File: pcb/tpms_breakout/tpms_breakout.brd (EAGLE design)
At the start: 50.8 x 61 mm, 21 parts, among them P1 53398-0410, P2 53398-0410, P3 53398-0410, P4 53398-0410, P5 53398-0410, P6 53398-0410, P7 53398-0410, P8 53398-0410, P9 53398-0610

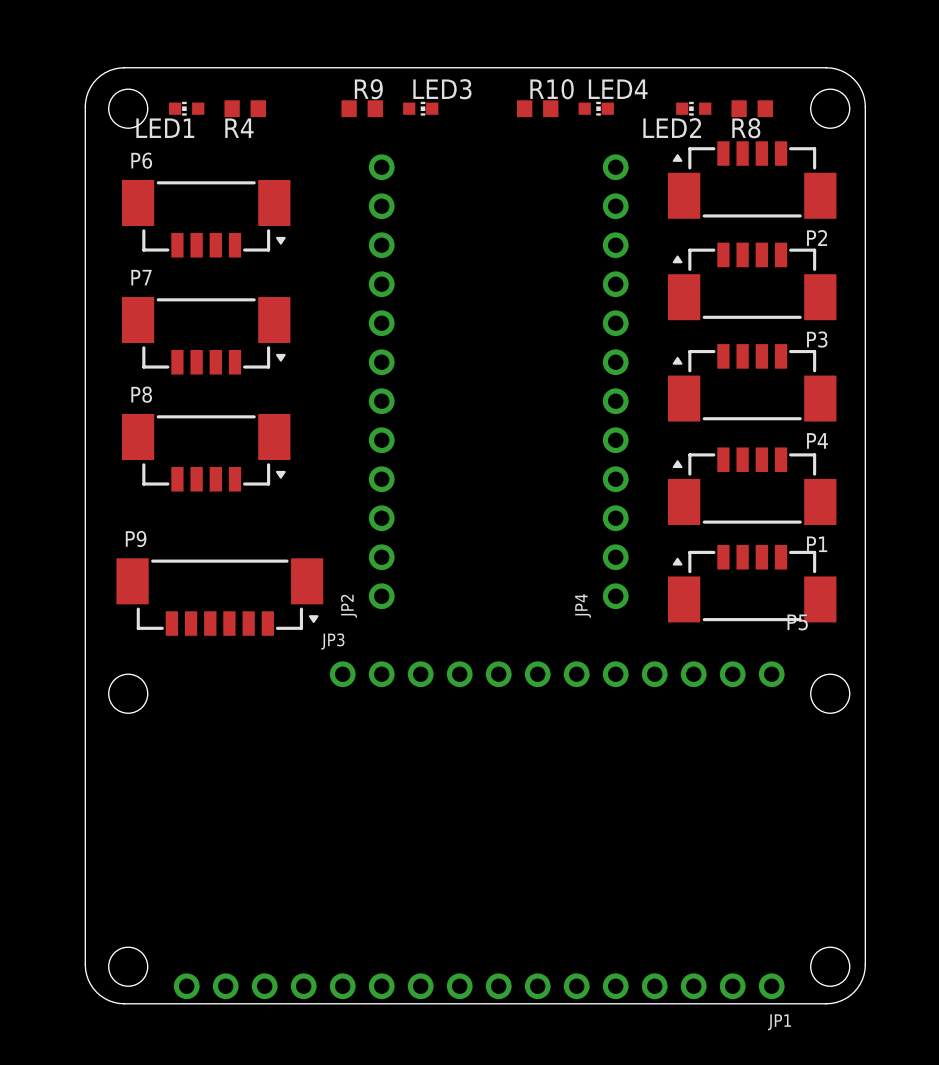
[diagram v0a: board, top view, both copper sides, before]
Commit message: initial versions of imu logger, cdh, and tpms pcb
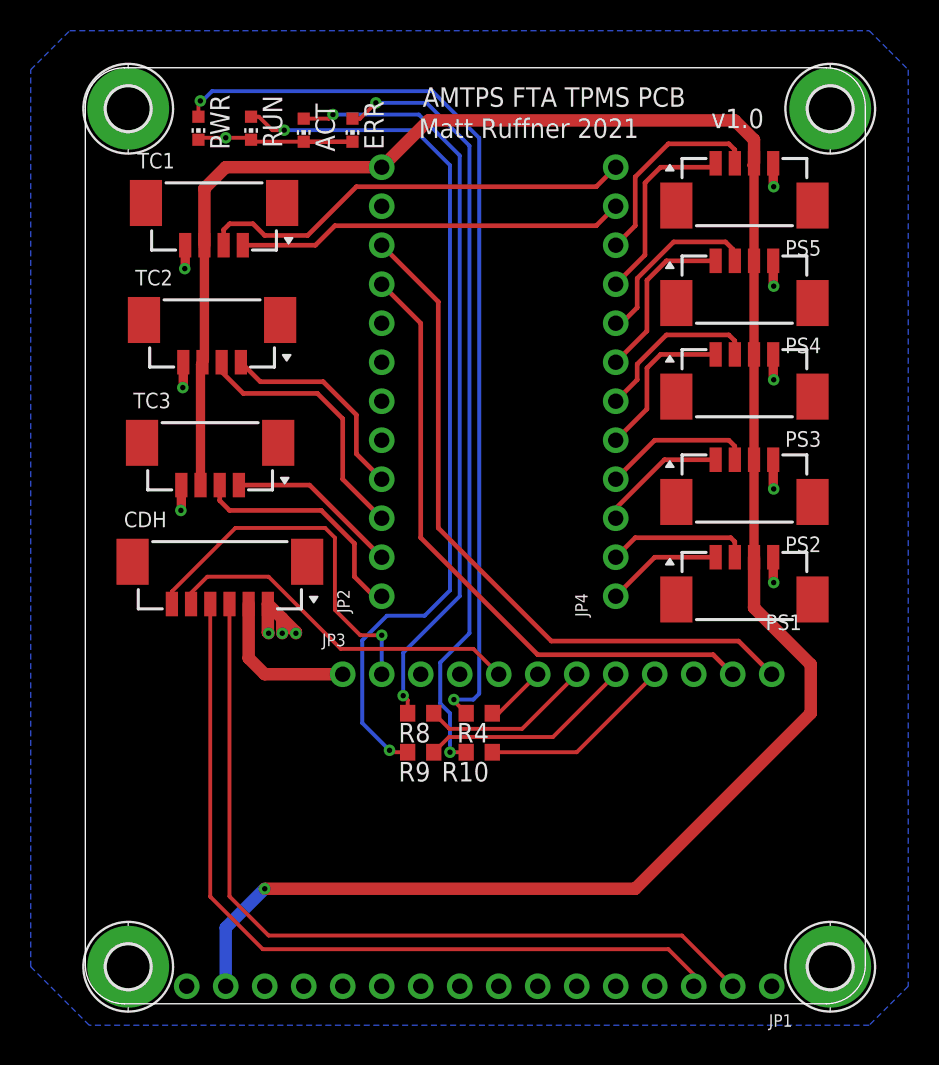
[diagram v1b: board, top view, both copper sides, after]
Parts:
- removed LED1, LED2, LED3, LED4: (no value), adafruit:CHIP-LED0603
- removed P1, P2, P3, P4, P5, P6, P7, P8: 53398-0410, con-molex-picoblade:53398-0410
- removed P9: 53398-0610, con-molex-picoblade:53398-0610
- added ACT, ERR, PWR, RUN: (no value), adafruit:CHIP-LED0603
- added CDH: 53398-0610, con-molex-picoblade:53398-0610
- added H1, H2, H3, H4: MOUNT-PAD-ROUND2.8, holes:2,8-PAD
- added PS1, PS2, PS3, PS4, PS5, TC1, TC2, TC3: 53398-0410, con-molex-picoblade:53398-0410
- moved R8 44.9 mm to (21.6, 19.1)
- moved R4 42.2 mm to (25.4, 19.1)
- moved R10 42.1 mm to (25.4, 16.5), turned to 180 degrees
- moved R9 42.1 mm to (21.6, 16.5), turned to 180 degrees
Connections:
- removed net +3V3: JP1.15
- removed net D0: JP1.3
- removed net D1: JP1.2
- removed net D10: JP3.7
- removed net D11: JP3.6
- removed net D12: JP3.5
- removed net D6: JP3.9
- removed net D9: JP3.8
- removed net N$1: P9.1
- removed net N$10: P9.6
- removed net N$2: P9.2
- removed net N$3: P9.3
- removed net N$4: P9.4
- removed net N$9: P9.5
- new net RX1: CDH.4, JP1.3
- new net SCHED: CDH.5, JP3.5
- new net TX1: CDH.3, JP1.2
- net 3V3: now also JP1.15, PS1.3, PS2.3, PS3.3, PS4.3, PS5.3, TC1.3, TC2.3, TC3.3; no longer P1.3, P2.3, P3.3, P4.3, P5.3, P6.3, P7.3, P8.3
- net EN: now also CDH.6
- net GND: now also ACT.C, CDH.1, ERR.C, H1.B2,8, H2.B2,8, H3.B2,8, H4.B2,8, PS1.4, PS2.4, PS3.4, PS4.4, PS5.4, PWR.C, RUN.C, TC1.4, TC2.4, TC3.4; no longer LED1.C, LED2.C, LED3.C, LED4.C, P1.4, P2.4, P3.4, P4.4, P5.4, P6.4, P7.4, P8.4
- net LED1: now also JP3.6
- net LED2: now also JP3.7
- net LED3: now also JP3.8
- net LED4: now also JP3.9
- net N$20: now also PWR.A; no longer LED1.A
- net N$21: now also ACT.A; no longer LED2.A
- net N$22: now also RUN.A; no longer LED3.A
- net N$23: now also ERR.A; no longer LED4.A
- net SC0: now also TC2.2
- net SC1: now also TC3.2
- net SC2: now also PS1.2; no longer P5.2
- net SC3: now also PS2.2
- net SC4: now also PS3.2
- net SC5: now also PS4.2
- net SC6: now also PS5.2
- net SC7: now also TC1.2
- net SD0: now also TC2.1
- net SD1: now also TC3.1
- net SD2: now also PS1.1; no longer P5.1
- net SD3: now also PS2.1
- net SD4: now also PS3.1
- net SD5: now also PS4.1
- net SD6: now also PS5.1
- net SD7: now also TC1.1
- net VBAT: now also CDH.2
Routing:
- net 3V3: track 0.00 -> 144.3 mm, vias 0 -> 1
- net N$20: track 0.00 -> 60.0 mm, vias 0 -> 2
- net N$22: track 0.00 -> 58.1 mm, vias 0 -> 2
- net TX1: track 0.00 -> 54.2 mm
- net RX1: track 0.00 -> 53.4 mm
- net N$23: track 0.00 -> 50.8 mm, vias 0 -> 2
- net N$21: track 0.00 -> 49.3 mm, vias 0 -> 2
- net SDA: track 0.00 -> 45.6 mm
- net SCL: track 0.00 -> 41.6 mm
- net GND: track 0.00 -> 32.2 mm, vias 0 -> 12
- net SC7: track 0.00 -> 28.9 mm
- net SD7: track 0.00 -> 25.3 mm
- net EN: track 0.00 -> 24.4 mm, vias 0 -> 1
- net SCHED: track 0.00 -> 23.9 mm
- net SC0: track 0.00 -> 17.3 mm
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- added copper zone on layer 16, net GND
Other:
- outline, holes or cut-outs redrawn
- board text added: "AMTPS FTA TPMS PCB"
- board text added: "Matt Ruffner 2021"
- board text added: "v1.0"

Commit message: finished TPMS board and other updates
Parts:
- moved R8 0.51 mm to (21.1, 19.1), flipped to the bottom, turned to 0 degrees
- flipped R10 to the bottom, turned to 0 degrees
- flipped R4 to the bottom, turned to 0 degrees
- flipped R9 to the bottom, turned to 0 degrees
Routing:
- net N$20: track 60.0 -> 58.6 mm, vias 2 -> 1
- net LED3: track 14.0 -> 14.7 mm, vias 0 -> 1
- net N$23: track 50.8 -> 50.2 mm, vias 2 -> 1
- net N$22: track 58.1 -> 57.5 mm, vias 2 -> 1
- net LED2: track 11.2 -> 11.8 mm, vias 0 -> 1
- net N$21: vias 2 -> 1
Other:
- board text added: "G 3V SC SD"
- board text added: "SD SC 3V G"
